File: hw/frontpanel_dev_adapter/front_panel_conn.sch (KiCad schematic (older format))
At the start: 19 parts, among them J301 FFC_conn_14p, J302 FFC_conn_14p, J303 JST_S2B-PH-SM4-TB, M301 FFC_retention_clamp, M302 FFC_retention_clamp, Q301 DMG1012T, U301 TLV9051SIDBV

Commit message: "Frontpanel dev-adapter: change some component sizes, add Logo & 4x mounting holes"
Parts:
- removed M301, M302: FFC_retention_clamp, customlib_mj_fp:FFC_retention_clamp_14pin_7_5mm, symbol customlib_mj:FFC_retention_clamp
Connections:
- no-connect marks 4 -> 0
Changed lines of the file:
@@
 FancyBtn LED connector \n(PWM ctrl low-side; 5V/12V selectable V+)
-$Comp
-L customlib_mj:FFC_retention_clamp M301
-U 1 1 5F4700B4
-P 3600 3600
-F 0 "M301" H 3600 3825 50  0000 C CNN
-F 1 "FFC_retention_clamp" H 3600 3734 50  0000 C CNN
-F 2 "customlib_mj_fp:FFC_retention_clamp_14pin_7_5mm" H 3600 3600 50  0001 C CNN
-F 3 "" H 3600 3600 50  0001 C CNN
-	1    3600 3600
-	1    0    0    -1
-$EndComp
-$Comp
-L customlib_mj:FFC_retention_clamp M302
-U 1 1 5F4709C2
-P 3600 6000
-F 0 "M302" H 3600 6225 50  0000 C CNN
-F 1 "FFC_retention_clamp" H 3600 6134 50  0000 C CNN
-F 2 "customlib_mj_fp:FFC_retention_clamp_14pin_7_5mm" H 3600 6000 50  0001 C CNN
-F 3 "" H 3600 6000 50  0001 C CNN
-	1    3600 6000
-	1    0    0    -1
-$EndComp
 $Comp
 L Device:R_Small R308
@@
 Wire Wire Line
 	6050 5800 6050 5700
-$Comp
-L customlib_mj:DMG1012T Q301
-U 1 1 5F4241F8
-P 5950 6650
-F 0 "Q301" H 6156 6696 50  0000 L CNN
-F 1 "DMG1012T" H 6352 6605 50  0000 C CNN
-F 2 "customlib_mj_fp:SOT-523_handsoldering" H 6150 6750 50  0001 C CNN
-F 3 "https://www.diodes.com/assets/Datasheets/ds31783.pdf" H 5950 6650 50  0001 C CNN
-	1    5950 6650
-	1    0    0    -1
-$EndComp
 Wire Wire Line
 	6050 6450 6050 6250
@@
 Wire Wire Line
 	6050 6850 6050 6950
-$Comp
-L Device:R_Small R309
-U 1 1 5F43274E
-P 5650 6800
-F 0 "R309" H 5709 6846 50  0000 L CNN
-F 1 "10k" H 5709 6755 50  0000 L CNN
-F 2 "Resistor_SMD:R_0603_1608Metric" H 5650 6800 50  0001 C CNN
-F 3 "~" H 5650 6800 50  0001 C CNN
-	1    5650 6800
-	1    0    0    -1
-$EndComp
 $Comp
 L power:GND #PWR0312
@@
 	1    0    0    -1
 $EndComp
-NoConn ~ 3500 3600
-NoConn ~ 3700 3600
-NoConn ~ 3500 6000
-NoConn ~ 3700 6000
 $Sheet
 S 9850 900  500  550
@@
 F3 "Tacho" O L 9850 1200 50
 $EndSheet
+$Comp
+L customlib_mj:DMG1012T Q301
+U 1 1 5F4241F8
+P 5950 6650
+F 0 "Q301" H 6156 6696 50  0000 L CNN
+F 1 "DMG1012T" H 6352 6605 50  0000 C CNN
+F 2 "customlib_mj_fp:SOT-523_handsoldering" H 6150 6750 50  0001 C CNN
+F 3 "https://www.diodes.com/assets/Datasheets/ds31783.pdf" H 5950 6650 50  0001 C CNN
+	1    5950 6650
+	1    0    0    -1
+$EndComp
+$Comp
+L Device:R_Small R309
+U 1 1 5F43274E
+P 5650 6800
+F 0 "R309" H 5709 6846 50  0000 L CNN
+F 1 "10k" H 5709 6755 50  0000 L CNN
+F 2 "Resistor_SMD:R_0603_1608Metric" H 5650 6800 50  0001 C CNN
+F 3 "~" H 5650 6800 50  0001 C CNN
+	1    5650 6800
+	1    0    0    -1
+$EndComp
 $EndSCHEMATC

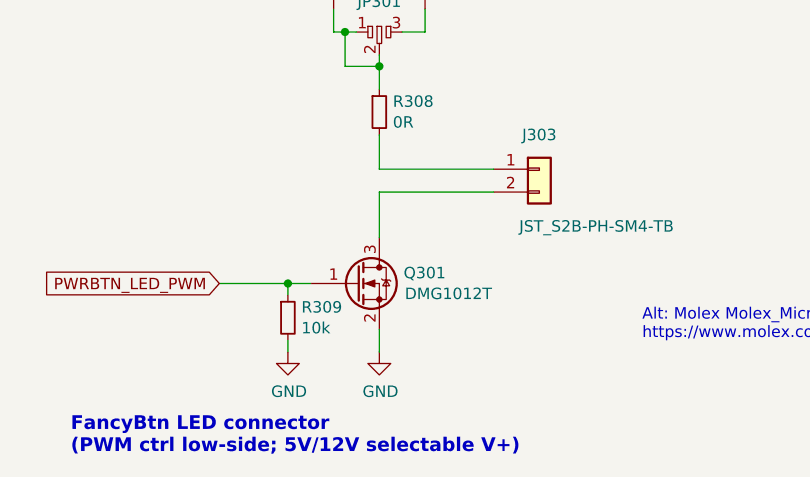
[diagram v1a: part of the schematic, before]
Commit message: Frontpanel dev adapter: Optimize some LCSC components for JLC assembly; add some datasheets. Optimize F103 16MHz xtal routing
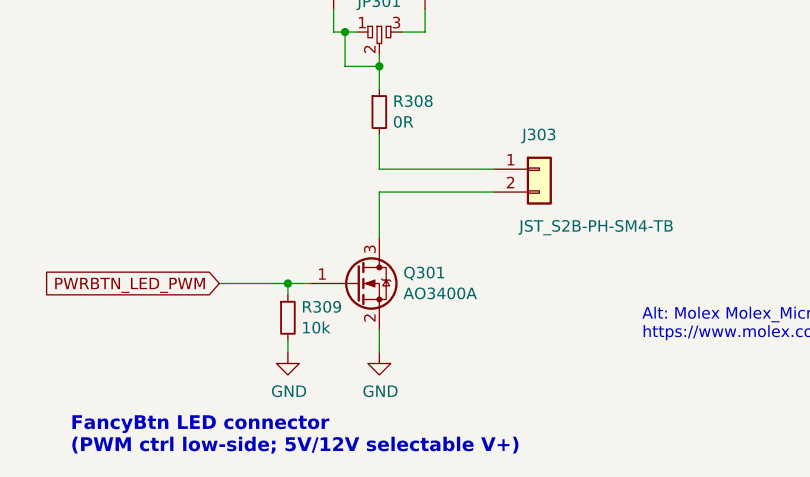
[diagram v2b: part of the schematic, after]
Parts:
- removed Q301: DMG1012T, customlib_mj_fp:SOT-523_handsoldering, symbol customlib_mj:DMG1012T
- added Q301: AO3400A, Package_TO_SOT_SMD:SOT-23, symbol Transistor_FET:AO3400A
- C301, C302: footprint Capacitor_SMD:C_0603_1608Metric -> Capacitor_SMD:C_0402_1005Metric
- R301, R302, R303, R306, R307, R308, R309: footprint Resistor_SMD:R_0603_1608Metric -> Resistor_SMD:R_0402_1005Metric
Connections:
- net GND: now also Q301.2 (S)
- net PWRBTN_LED_PWM: now also Q301.1 (G)
- net at J303.2 (Pin_2): now also Q301.3 (D)
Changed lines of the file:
@@
 F 0 "R308" H 6109 5946 50  0000 L CNN
 F 1 "0R" H 6109 5855 50  0000 L CNN
-F 2 "Resistor_SMD:R_0603_1608Metric" H 6050 5900 50  0001 C CNN
+F 2 "Resistor_SMD:R_0402_1005Metric" H 6050 5900 50  0001 C CNN
 F 3 "~" H 6050 5900 50  0001 C CNN
 	1    6050 5900
@@
 F 0 "R302" H 4550 1050 50  0000 L CNN
 F 1 "10k" H 4550 950 50  0000 L CNN
-F 2 "Resistor_SMD:R_0603_1608Metric" H 4500 1000 50  0001 C CNN
+F 2 "Resistor_SMD:R_0402_1005Metric" H 4500 1000 50  0001 C CNN
 F 3 "~" H 4500 1000 50  0001 C CNN
 	1    4500 1000
@@
 F 0 "R301" V 5375 950 50  0000 L CNN
 F 1 "20k" V 5300 875 50  0000 L CNN
-F 2 "Resistor_SMD:R_0603_1608Metric" H 5300 950 50  0001 C CNN
+F 2 "Resistor_SMD:R_0402_1005Metric" H 5300 950 50  0001 C CNN
 F 3 "~" H 5300 950 50  0001 C CNN
 	1    5300 950
@@
 F 0 "R306" V 5225 1050 50  0000 L CNN
 F 1 "20k" V 5300 975 50  0000 L CNN
-F 2 "Resistor_SMD:R_0603_1608Metric" H 5300 1050 50  0001 C CNN
+F 2 "Resistor_SMD:R_0402_1005Metric" H 5300 1050 50  0001 C CNN
 F 3 "~" H 5300 1050 50  0001 C CNN
 	1    5300 1050
@@
 F 0 "R303" H 4900 1050 50  0000 L CNN
 F 1 "20k" H 4900 950 50  0000 L CNN
-F 2 "Resistor_SMD:R_0603_1608Metric" H 4850 1000 50  0001 C CNN
+F 2 "Resistor_SMD:R_0402_1005Metric" H 4850 1000 50  0001 C CNN
 F 3 "~" H 4850 1000 50  0001 C CNN
 	1    4850 1000
@@
 F 0 "R307" H 5250 1550 50  0000 L CNN
 F 1 "27k" H 5250 1450 50  0000 L CNN
-F 2 "Resistor_SMD:R_0603_1608Metric" H 5200 1500 50  0001 C CNN
+F 2 "Resistor_SMD:R_0402_1005Metric" H 5200 1500 50  0001 C CNN
 F 3 "~" H 5200 1500 50  0001 C CNN
 	1    5200 1500
@@
 F 0 "C302" H 4714 1454 50  0000 L CNN
 F 1 "100n" H 4714 1545 50  0000 L CNN
-F 2 "Capacitor_SMD:C_0603_1608Metric" H 5000 1500 50  0001 C CNN
+F 2 "Capacitor_SMD:C_0402_1005Metric" H 5000 1500 50  0001 C CNN
 F 3 "~" H 5000 1500 50  0001 C CNN
 	1    5000 1500
@@
 F 0 "C301" H 8242 1296 50  0000 L CNN
 F 1 "100n" H 8242 1205 50  0000 L CNN
-F 2 "Capacitor_SMD:C_0603_1608Metric" H 8150 1250 50  0001 C CNN
+F 2 "Capacitor_SMD:C_0402_1005Metric" H 8150 1250 50  0001 C CNN
 F 3 "~" H 8150 1250 50  0001 C CNN
 	1    8150 1250
@@
 $EndSheet
 $Comp
-L customlib_mj:DMG1012T Q301
-U 1 1 5F4241F8
-P 5950 6650
-F 0 "Q301" H 6156 6696 50  0000 L CNN
-F 1 "DMG1012T" H 6352 6605 50  0000 C CNN
-F 2 "customlib_mj_fp:SOT-523_handsoldering" H 6150 6750 50  0001 C CNN
-F 3 "https://www.diodes.com/assets/Datasheets/ds31783.pdf" H 5950 6650 50  0001 C CNN
-	1    5950 6650
-	1    0    0    -1
-$EndComp
-$Comp
 L Device:R_Small R309
 U 1 1 5F43274E
@@
 F 0 "R309" H 5709 6846 50  0000 L CNN
 F 1 "10k" H 5709 6755 50  0000 L CNN
-F 2 "Resistor_SMD:R_0603_1608Metric" H 5650 6800 50  0001 C CNN
+F 2 "Resistor_SMD:R_0402_1005Metric" H 5650 6800 50  0001 C CNN
 F 3 "~" H 5650 6800 50  0001 C CNN
 	1    5650 6800
 	1    0    0    -1
 $EndComp
+$Comp
+L Transistor_FET:AO3400A Q301
+U 1 1 60342B42
+P 5950 6650
+F 0 "Q301" H 6155 6696 50  0000 L CNN
+F 1 "AO3400A" H 6155 6605 50  0000 L CNN
+F 2 "Package_TO_SOT_SMD:SOT-23" H 6150 6575 50  0001 L CIN
+F 3 "http://www.aosmd.com/pdfs/datasheet/AO3400A.pdf" H 5950 6650 50  0001 L CNN
+	1    5950 6650
+	1    0    0    -1
+$EndComp

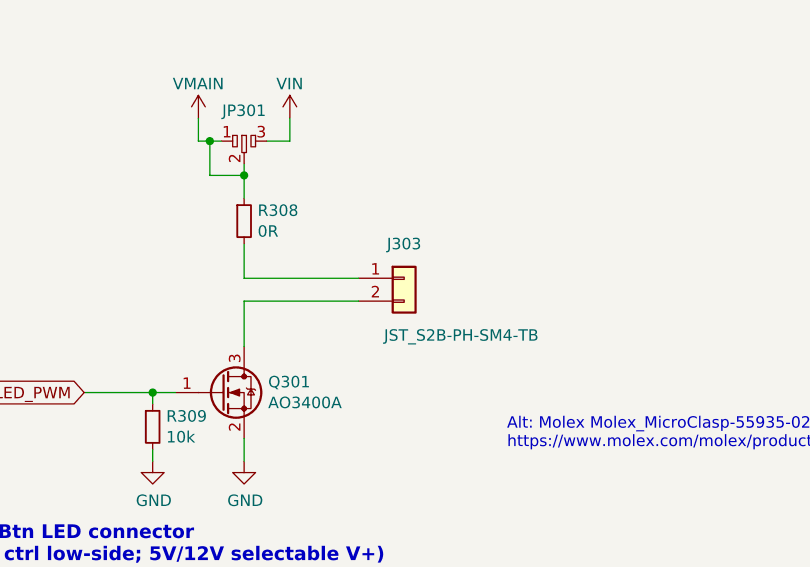
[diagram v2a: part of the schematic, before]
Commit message: FP adapter board: Added LCSC partnumbers to all components to be PnP:ed; Finalized some silk additions; Generated Gerbers, BoM & pnp-files for JCL assembly
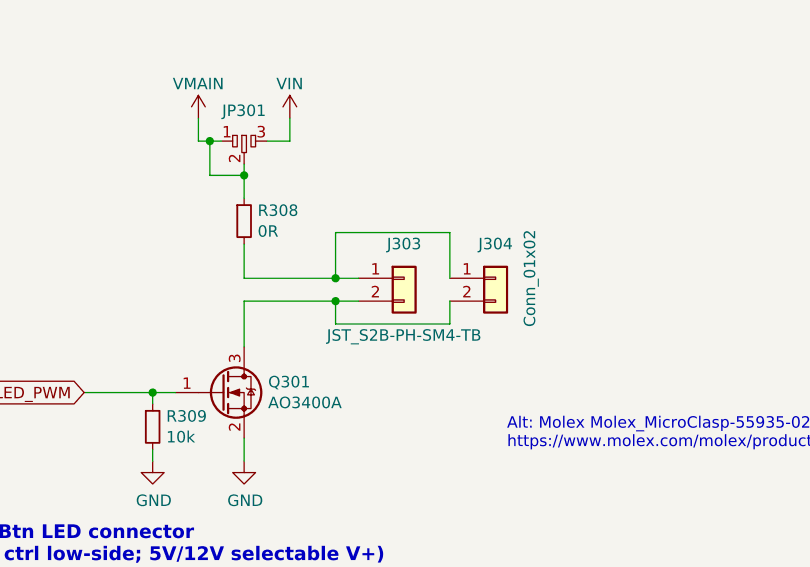
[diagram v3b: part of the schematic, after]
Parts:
- added J304: Conn_01x02, Connector_PinHeader_2.54mm:PinHeader_1x02_P2.54mm_Vertical, symbol Connector_Generic:Conn_01x02
- C301, C302: LCSC (none) -> C1525
- Q301: LCSC (none) -> C20917
- R301, R303, R306: LCSC (none) -> C25765
- R302, R309: LCSC (none) -> C25744
- R304, R305: LCSC (none) -> C22813
- R307: LCSC (none) -> C25771
- R308: LCSC (none) -> C17168
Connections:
- net at J303.1 (Pin_1), R308.2: now also J304.1 (Pin_1)
- net at J303.2 (Pin_2), Q301.3 (D): now also J304.2 (Pin_2)
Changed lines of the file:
@@
 P 6750 6150
 F 0 "J303" H 6750 6300 50  0000 C CNN
-F 1 "JST_S2B-PH-SM4-TB" H 7000 5900 50  0000 C CNN
+F 1 "JST_S2B-PH-SM4-TB" H 6750 5900 50  0000 C CNN
 F 2 "customlib_mj_fp:JST_PH_S2B-PH-SM4-TB_1x02-1MP_P2.00mm_Horizontal" H 6750 6150 50  0001 C CNN
 F 3 "" H 6750 6150 50  0001 C CNN
@@
 F 2 "Resistor_SMD:R_0402_1005Metric" H 6050 5900 50  0001 C CNN
 F 3 "~" H 6050 5900 50  0001 C CNN
+F 4 "C17168" H 6050 5900 50  0001 C CNN "LCSC"
 	1    6050 5900
 	1    0    0    -1
@@
 F 2 "Resistor_SMD:R_0402_1005Metric" H 4500 1000 50  0001 C CNN
 F 3 "~" H 4500 1000 50  0001 C CNN
+F 4 "C25744" H 4500 1000 50  0001 C CNN "LCSC"
 	1    4500 1000
 	1    0    0    -1
@@
 F 2 "Resistor_SMD:R_0402_1005Metric" H 5300 950 50  0001 C CNN
 F 3 "~" H 5300 950 50  0001 C CNN
+F 4 "C25765" V 5300 950 50  0001 C CNN "LCSC"
 	1    5300 950
 	0    -1   -1   0
@@
 F 2 "Resistor_SMD:R_0402_1005Metric" H 5300 1050 50  0001 C CNN
 F 3 "~" H 5300 1050 50  0001 C CNN
+F 4 "C25765" V 5300 1050 50  0001 C CNN "LCSC"
 	1    5300 1050
 	0    -1   -1   0
@@
 F 2 "Resistor_SMD:R_0402_1005Metric" H 4850 1000 50  0001 C CNN
 F 3 "~" H 4850 1000 50  0001 C CNN
+F 4 "C25765" H 4850 1000 50  0001 C CNN "LCSC"
 	1    4850 1000
 	1    0    0    -1
@@
 F 2 "Resistor_SMD:R_0603_1608Metric" H 5900 1000 50  0001 C CNN
 F 3 "~" H 5900 1000 50  0001 C CNN
+F 4 "C22813" H 5900 1000 50  0001 C CNN "LCSC"
 	1    5900 1000
 	1    0    0    -1
@@
 F 2 "Resistor_SMD:R_0603_1608Metric" H 5800 1000 50  0001 C CNN
 F 3 "~" H 5800 1000 50  0001 C CNN
+F 4 "C22813" H 5800 1000 50  0001 C CNN "LCSC"
 	1    5800 1000
 	-1   0    0    -1
@@
 F 2 "Resistor_SMD:R_0402_1005Metric" H 5200 1500 50  0001 C CNN
 F 3 "~" H 5200 1500 50  0001 C CNN
+F 4 "C25771" H 5200 1500 50  0001 C CNN "LCSC"
 	1    5200 1500
 	1    0    0    -1
@@
 F 2 "Capacitor_SMD:C_0402_1005Metric" H 5000 1500 50  0001 C CNN
 F 3 "~" H 5000 1500 50  0001 C CNN
+F 4 "C1525" H 5000 1500 50  0001 C CNN "LCSC"
 	1    5000 1500
 	1    0    0    1
@@
 F 2 "Capacitor_SMD:C_0402_1005Metric" H 8150 1250 50  0001 C CNN
 F 3 "~" H 8150 1250 50  0001 C CNN
+F 4 "C1525" H 8150 1250 50  0001 C CNN "LCSC"
 	1    8150 1250
 	1    0    0    -1
@@
 F 2 "Package_TO_SOT_SMD:TSOT-23-6" H 6800 1100 50  0001 C CNN
 F 3 "https://www.ti.com/lit/gpn/tlv9051" H 6850 1300 50  0001 C CNN
+F 4 "" H 6800 1100 50  0001 C CNN "LCSC"
 	1    6800 1100
 	1    0    0    1
@@
 	6050 6000 6050 6150
 Wire Wire Line
-	6050 6150 6550 6150
+	6050 6150 6450 6150
 Wire Wire Line
 	6050 5800 6050 5700
@@
 	6050 6450 6050 6250
 Wire Wire Line
-	6050 6250 6550 6250
+	6050 6250 6450 6250
 $Comp
 L power:GND #PWR0313
@@
 F 2 "Resistor_SMD:R_0402_1005Metric" H 5650 6800 50  0001 C CNN
 F 3 "~" H 5650 6800 50  0001 C CNN
+F 4 "C25744" H 5650 6800 50  0001 C CNN "LCSC"
 	1    5650 6800
 	1    0    0    -1
@@
 F 2 "Package_TO_SOT_SMD:SOT-23" H 6150 6575 50  0001 L CIN
 F 3 "http://www.aosmd.com/pdfs/datasheet/AO3400A.pdf" H 5950 6650 50  0001 L CNN
+F 4 "C20917" H 5950 6650 50  0001 C CNN "LCSC"
 	1    5950 6650
 	1    0    0    -1
 $EndComp
+$Comp
+L Connector_Generic:Conn_01x02 J304
+U 1 1 6093533B
+P 7150 6150
+F 0 "J304" H 7150 6300 50  0000 C CNN
+F 1 "Conn_01x02" V 7300 6150 50  0000 C CNN
+F 2 "Connector_PinHeader_2.54mm:PinHeader_1x02_P2.54mm_Vertical" H 7150 6150 50  0001 C CNN
+F 3 "~" H 7150 6150 50  0001 C CNN
+	1    7150 6150
+	1    0    0    -1
+$EndComp
+Wire Wire Line
+	6450 6150 6450 5950
+Wire Wire Line
+	6450 5950 6950 5950
+Wire Wire Line
+	6950 5950 6950 6150
+Connection ~ 6450 6150
+Wire Wire Line
+	6450 6150 6550 6150
+Wire Wire Line
+	6450 6250 6450 6350
+Wire Wire Line
+	6450 6350 6950 6350
+Wire Wire Line
+	6950 6350 6950 6250
+Connection ~ 6450 6250
+Wire Wire Line
+	6450 6250 6550 6250
 $EndSCHEMATC
